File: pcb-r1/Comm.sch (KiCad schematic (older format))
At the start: 14 parts, among them P201 CONN_01X06, P202 CONN_01X04, P203 CONN_01X04, P204 CONN_01X03, SW201 TL3315NF160Q

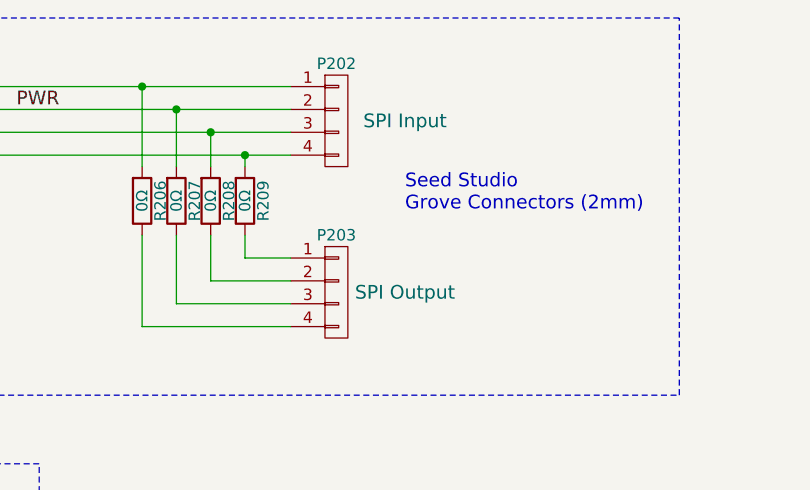
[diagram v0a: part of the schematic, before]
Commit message: Generated the final Gerbers for fabrication
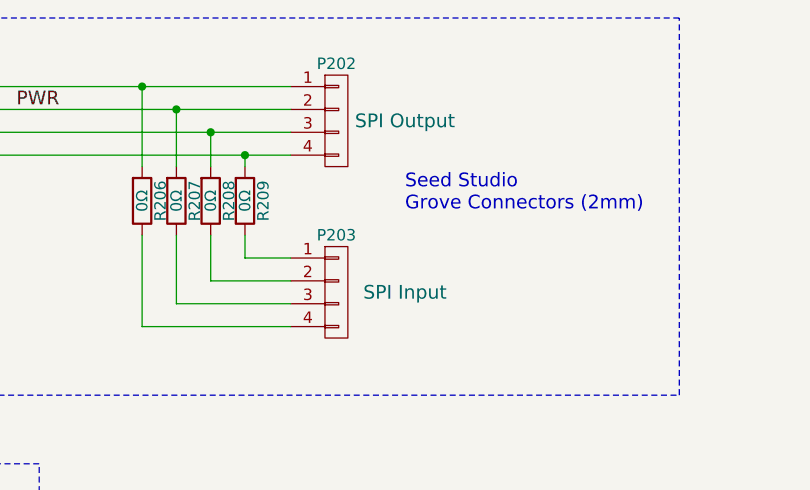
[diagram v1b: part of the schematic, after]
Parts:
- P202: Label SPI Input -> SPI Output
- P203: Label SPI Output -> SPI Input
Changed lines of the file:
@@
 F 4 "Value" H 4900 1200 60  0001 C CNN "MPN"
 F 5 "Value" H 4900 1200 60  0001 C CNN "ConradPN"
-F 6 "SPI Input" H 5200 1200 60  0000 C CNN "Label"
+F 6 "SPI Output" H 5200 1200 60  0000 C CNN "Label"
 	1    4900 1200
 	1    0    0    -1
@@
 F 4 "Value" H 4900 1950 60  0001 C CNN "MPN"
 F 5 "Value" H 4900 1950 60  0001 C CNN "ConradPN"
-F 6 "SPI Output" H 5200 1950 60  0000 C CNN "Label"
+F 6 "SPI Input" H 5200 1950 60  0000 C CNN "Label"
 	1    4900 1950
 	1    0    0    -1

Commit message: Preparing the BOM
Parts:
- C201: value C -> 0.1μF
- R201, R202: value R -> 0Ω
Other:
- note added: "TODO - Verify the value of C201"
- note added: "TODO - Verify the values of R201 and R202"
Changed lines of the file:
@@
 P 1950 6450
 F 0 "C201" H 1975 6550 50  0000 L CNN
-F 1 "C" H 1975 6350 50  0000 L CNN
+F 1 "0.1μF" H 1975 6350 50  0000 L CNN
 F 2 "Capacitors_SMD:C_0805" H 1988 6300 30  0001 C CNN
 F 3 "" H 1950 6450 60  0000 C CNN
@@
 P 2300 3250
 F 0 "R201" V 2380 3250 50  0000 C CNN
-F 1 "R" V 2300 3250 50  0000 C CNN
+F 1 "0Ω" V 2300 3250 50  0000 C CNN
 F 2 "Resistors_SMD:R_0805" V 2230 3250 30  0001 C CNN
 F 3 "" H 2300 3250 30  0000 C CNN
@@
 P 2300 3900
 F 0 "R202" V 2380 3900 50  0000 C CNN
-F 1 "R" V 2300 3900 50  0000 C CNN
+F 1 "0Ω" V 2300 3900 50  0000 C CNN
 F 2 "Resistors_SMD:R_0805" V 2230 3900 30  0001 C CNN
 F 3 "" H 2300 3900 30  0000 C CNN
@@
 	4050 1400 4050 1050
 Connection ~ 4050 1050
+Text Notes 1100 2650 0    60   ~ 0
+TODO - Verify the values of R201 and R202
+Text Notes 1430 5800 0    60   ~ 0
+TODO - Verify the value of C201
 $EndSCHEMATC

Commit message: Updated the parts for the BOM
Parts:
- SW201: ConradPN (none) -> Value; DigiKeyPN (none) -> FSM2JSMAA-ND; Label (none) -> Value; MPN (none) -> FSM2JSMAA
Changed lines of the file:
@@
 F 2 "CentralCommand:PTS525SM15SMTR2LFS" H 2350 6400 60  0001 C CNN
 F 3 "" H 2350 6400 60  0000 C CNN
+F 4 "FSM2JSMAA" H 2350 6450 60  0001 C CNN "MPN"
+F 5 "Value" H 2350 6450 60  0001 C CNN "ConradPN"
+F 6 "Value" H 2350 6450 60  0000 C CNN "Label"
+F 7 "FSM2JSMAA-ND" H 2350 6450 60  0001 C CNN "DigiKeyPN"
 	1    2350 6450
 	1    0    0    -1

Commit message: Updated the parts with further DigiKeyPN
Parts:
- C201: DigiKeyPN (none) -> 478-1395-1-ND
- P201: DigiKeyPN (none) -> 952-2247-ND
- R201, R202, R204: value 0Ω -> 10kΩ; DigiKeyPN (none) -> 311-10.0KCRCT-ND
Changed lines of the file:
@@
 F 2 "Capacitors_SMD:C_0805" H 1988 6300 30  0001 C CNN
 F 3 "" H 1950 6450 60  0000 C CNN
+F 4 "478-1395-1-ND" H 1950 6450 60  0001 C CNN "DigiKeyPN"
 	1    1950 6450
 	1    0    0    -1
@@
 P 2300 3250
 F 0 "R201" V 2380 3250 50  0000 C CNN
-F 1 "0Ω" V 2300 3250 50  0000 C CNN
+F 1 "10kΩ" V 2300 3250 50  0000 C CNN
 F 2 "Resistors_SMD:R_0805" V 2230 3250 30  0001 C CNN
 F 3 "" H 2300 3250 30  0000 C CNN
+F 4 "311-10.0KCRCT-ND" H 2300 3250 60  0001 C CNN "DigiKeyPN"
 	1    2300 3250
 	1    0    0    1
@@
 F 2 "Pin_Headers:Pin_Header_Straight_1x06" H 3300 3750 60  0001 C CNN
 F 3 "" H 3300 3750 60  0000 C CNN
+F 4 "952-2247-ND" H 3300 3750 60  0001 C CNN "DigiKeyPN"
 	1    3300 3750
 	1    0    0    -1
@@
 P 2300 3900
 F 0 "R202" V 2380 3900 50  0000 C CNN
-F 1 "0Ω" V 2300 3900 50  0000 C CNN
+F 1 "10kΩ" V 2300 3900 50  0000 C CNN
 F 2 "Resistors_SMD:R_0805" V 2230 3900 30  0001 C CNN
 F 3 "" H 2300 3900 30  0000 C CNN
+F 4 "311-10.0KCRCT-ND" H 2300 3900 60  0001 C CNN "DigiKeyPN"
 	1    2300 3900
 	1    0    0    1
@@
 P 3000 4500
 F 0 "R204" V 3080 4500 50  0000 C CNN
-F 1 "0Ω" V 3000 4500 50  0000 C CNN
+F 1 "10kΩ" V 3000 4500 50  0000 C CNN
 F 2 "Resistors_SMD:R_0805" V 2930 4500 30  0001 C CNN
 F 3 "" H 3000 4500 30  0000 C CNN
+F 4 "311-10.0KCRCT-ND" H 3000 4500 60  0001 C CNN "DigiKeyPN"
 	1    3000 4500
 	1    0    0    1
